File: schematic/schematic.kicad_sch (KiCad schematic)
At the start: 94 parts, among them J1 GATE_OUT_1, J10 CV_OUT_2, J11 FWD_CLK_IN, J12 BWD_CLK_IN, J13 RST_IN, J14 KBD_Gate_Out, J15 ZERO_IN, J2 GATE_OUT_2, J3 GATE_OUT_3, J4 GATE_OUT_4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

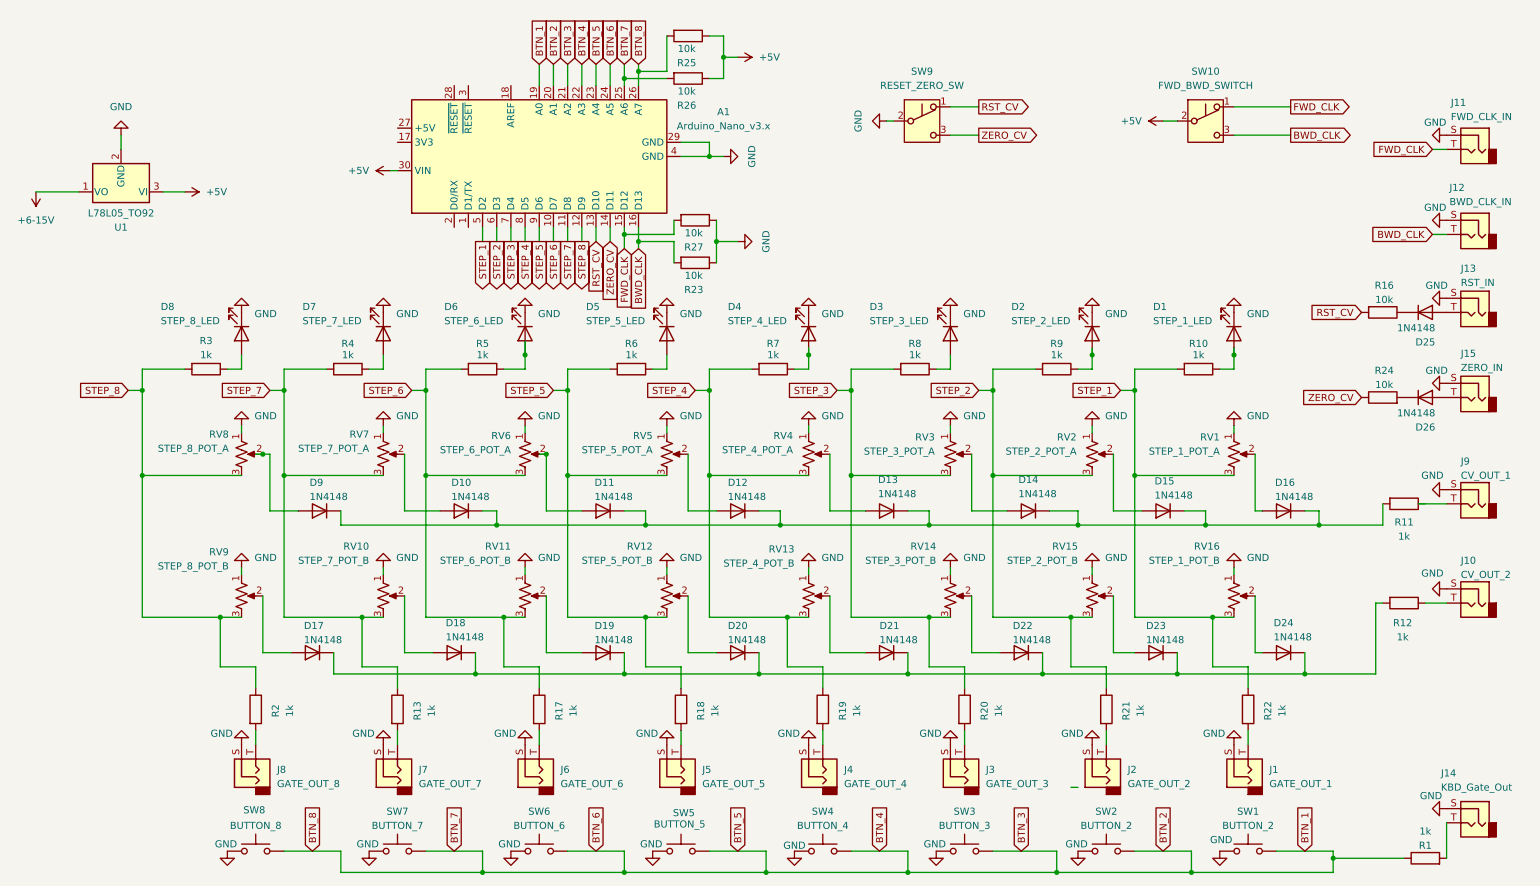
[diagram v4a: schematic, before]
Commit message: Add diodes to all inputs
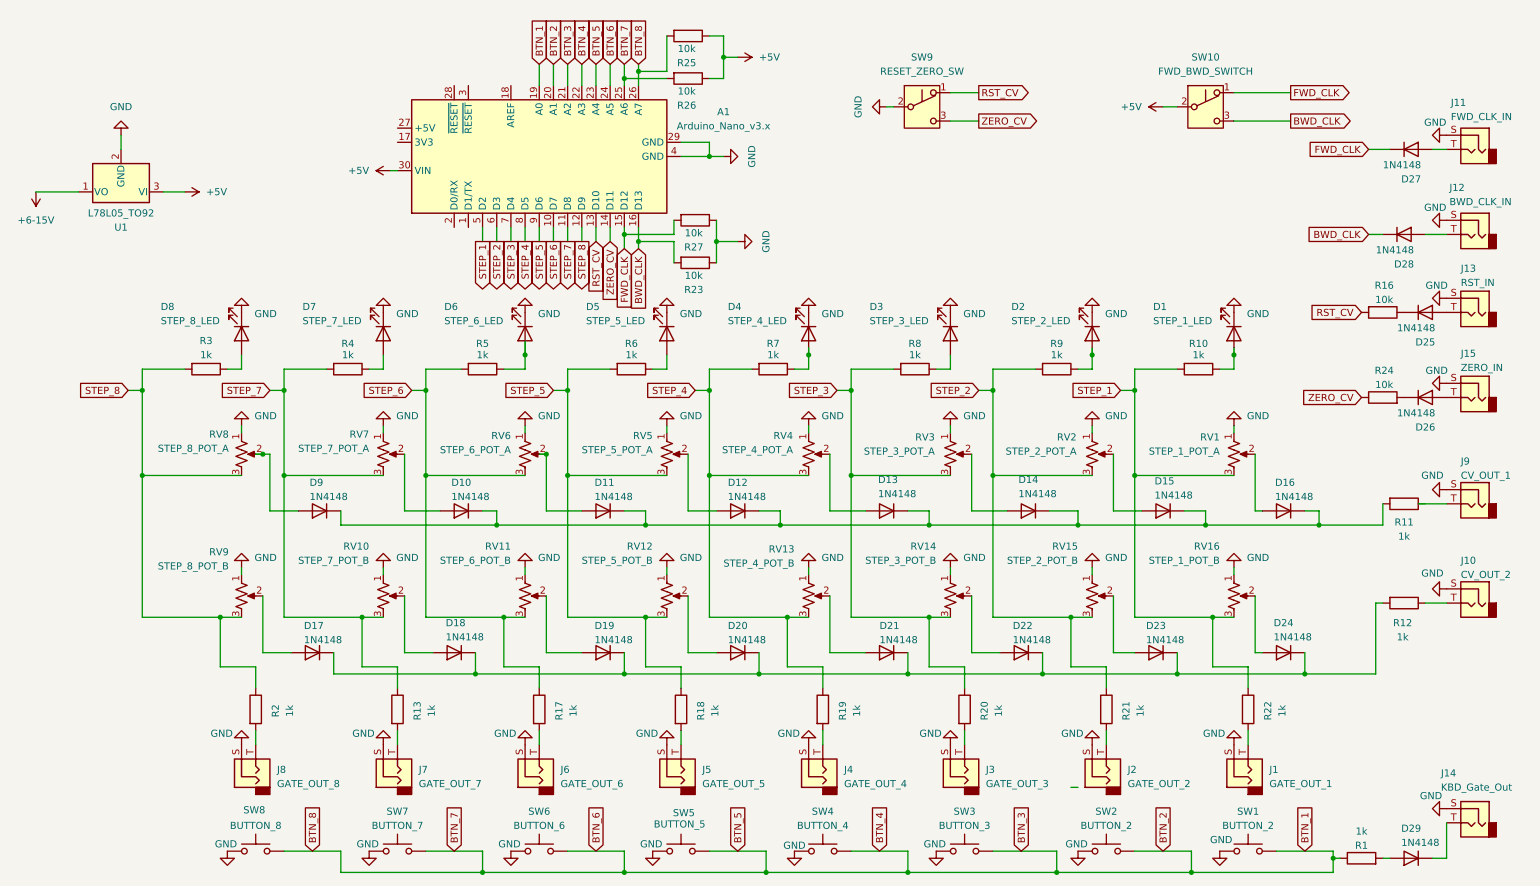
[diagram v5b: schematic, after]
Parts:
- added D27, D28, D29: 1N4148, Diode_THT:D_DO-35_SOD27_P7.62mm_Horizontal, symbol Diode:1N4148
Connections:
- net BWD_CLK: now also D28.1 (K); no longer J12.T
- net FWD_CLK: now also D27.1 (K); no longer J11.T
- net at J14.T: now also D29.1 (K); no longer R1.2
- new net: D27.2 (A), J11.T
- new net: D29.2 (A), R1.2
- new net: D28.2 (A), J12.T
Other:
- moved on the sheet: R1, SW10, SW9

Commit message: Cleanup and version schematic
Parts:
- SW10: value FWD_BWD_SWITCH -> FWD_BWD_SW
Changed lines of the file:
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@@
 	(title_block
 		(title "rustino-seq")
+		(date "2025-10-31")
+		(rev "1.0")
 	)
 	(junction
@@
 			)
 		)
-		(property "Value" "FWD_BWD_SWITCH"
+		(property "Value" "FWD_BWD_SW"
 			(at 228.6 21.59 0)
 			(effects
